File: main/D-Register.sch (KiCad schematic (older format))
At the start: 19 parts, among them U77 74LS245, U78 74LS173, U79 74LS173

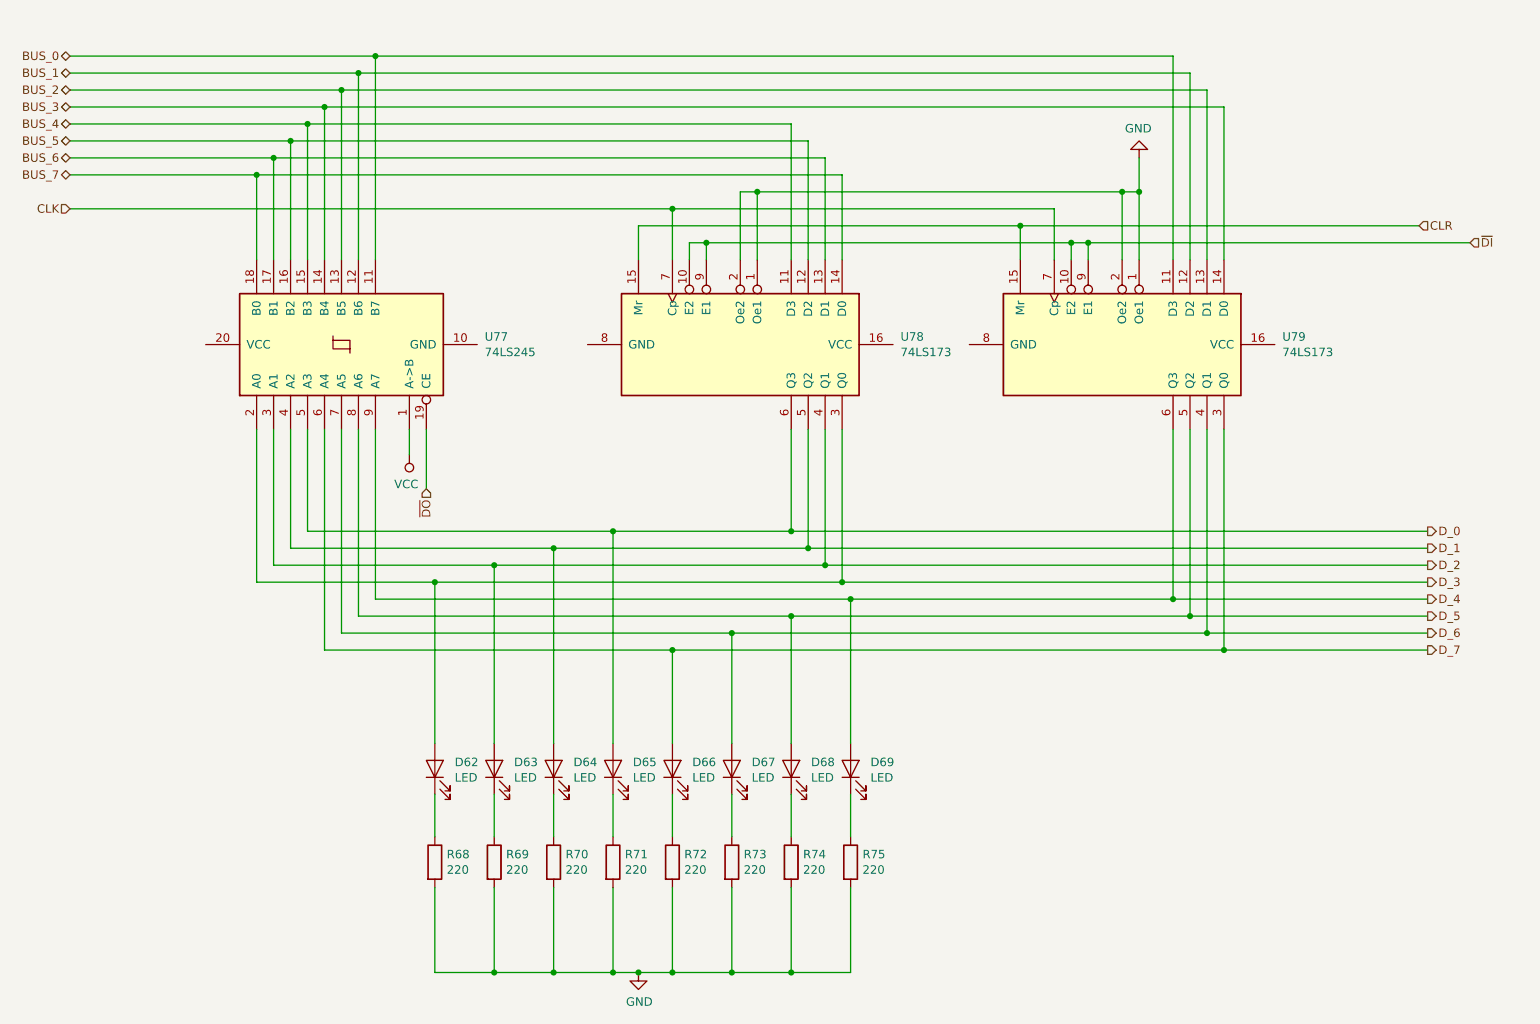
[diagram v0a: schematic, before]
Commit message: Replot main with symbols
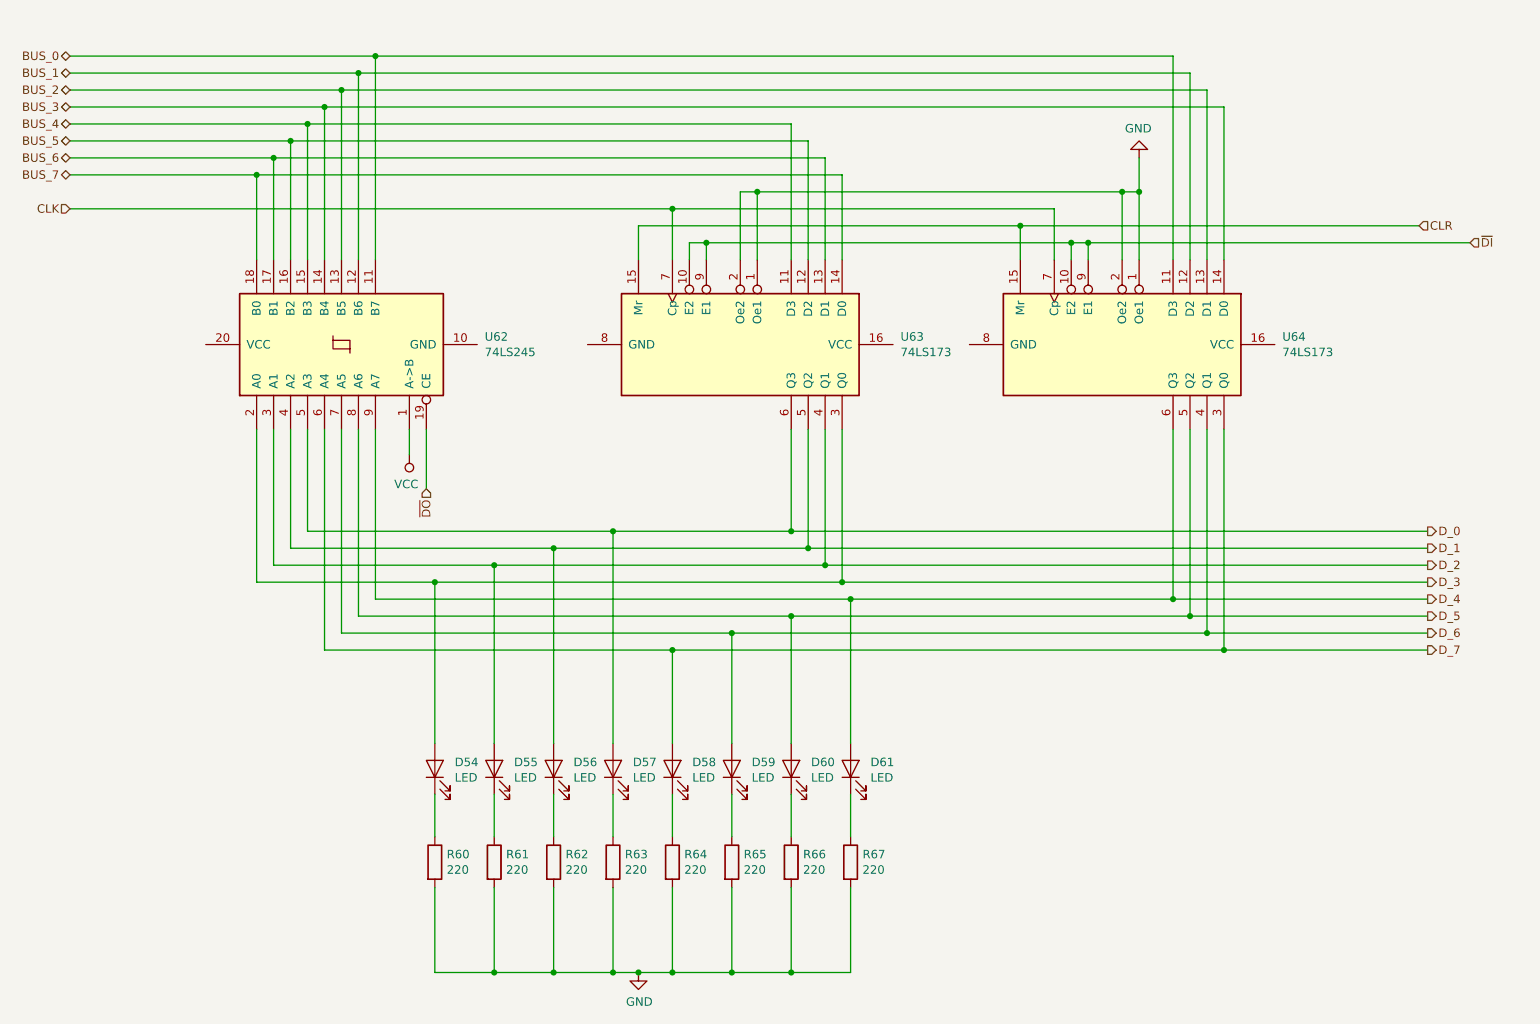
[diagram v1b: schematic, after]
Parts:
- renumbered D62 to D54, D63 to D55, D64 to D56, D65 to D57, D66 to D58, D67 to D59, D68 to D60, D69 to D61, R68 to R60, R69 to R61, R70 to R62, R71 to R63, R72 to R64, R73 to R65, R74 to R66, R75 to R67, U77 to U62, U78 to U63, U79 to U64
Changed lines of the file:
@@
 Sheet 17 26
 Title "D Register"
-Date "2019-11-13"
+Date "2019-11-17"
 Rev "v1.0"
 Comp "Christopher Milan"
@@
 AR Path="/5D9C73BD/5DA1765F" Ref="U?"  Part="1"
 AR Path="/5D9E82CE/5DA1765F" Ref="U?"  Part="1"
-AR Path="/5DA98D6D/5DA9A587/5DA1765F" Ref="U78"  Part="1"
-F 0 "U78" V 5204 4044 50  0000 L CNN
+AR Path="/5DA98D6D/5DA9A587/5DA1765F" Ref="U63"  Part="1"
+F 0 "U63" V 5204 4044 50  0000 L CNN
 F 1 "74LS173" V 5295 4044 50  0000 L CNN
 F 2 "" H 5250 3100 50  0001 C CNN
@@
 AR Path="/5D9C73BD/5DA1760E" Ref="R?"  Part="1"
 AR Path="/5D9E82CE/5DA1760E" Ref="R?"  Part="1"
-AR Path="/5DA98D6D/5DA9A587/5DA1760E" Ref="R75"  Part="1"
-F 0 "R75" H 5970 6196 50  0000 L CNN
+AR Path="/5DA98D6D/5DA9A587/5DA1760E" Ref="R67"  Part="1"
+F 0 "R67" H 5970 6196 50  0000 L CNN
 F 1 "220" H 5970 6105 50  0000 L CNN
 F 2 "" V 5830 6150 50  0001 C CNN
@@
 AR Path="/5D9C73BD/5DA17608" Ref="R?"  Part="1"
 AR Path="/5D9E82CE/5DA17608" Ref="R?"  Part="1"
-AR Path="/5DA98D6D/5DA9A587/5DA17608" Ref="R74"  Part="1"
-F 0 "R74" H 5620 6196 50  0000 L CNN
+AR Path="/5DA98D6D/5DA9A587/5DA17608" Ref="R66"  Part="1"
+F 0 "R66" H 5620 6196 50  0000 L CNN
 F 1 "220" H 5620 6105 50  0000 L CNN
 F 2 "" V 5480 6150 50  0001 C CNN
@@
 AR Path="/5D9C73BD/5DA17602" Ref="R?"  Part="1"
 AR Path="/5D9E82CE/5DA17602" Ref="R?"  Part="1"
-AR Path="/5DA98D6D/5DA9A587/5DA17602" Ref="R73"  Part="1"
-F 0 "R73" H 5270 6196 50  0000 L CNN
+AR Path="/5DA98D6D/5DA9A587/5DA17602" Ref="R65"  Part="1"
+F 0 "R65" H 5270 6196 50  0000 L CNN
 F 1 "220" H 5270 6105 50  0000 L CNN
 F 2 "" V 5130 6150 50  0001 C CNN
@@
 AR Path="/5D9C73BD/5DA175FC" Ref="R?"  Part="1"
 AR Path="/5D9E82CE/5DA175FC" Ref="R?"  Part="1"
-AR Path="/5DA98D6D/5DA9A587/5DA175FC" Ref="R72"  Part="1"
-F 0 "R72" H 4920 6196 50  0000 L CNN
+AR Path="/5DA98D6D/5DA9A587/5DA175FC" Ref="R64"  Part="1"
+F 0 "R64" H 4920 6196 50  0000 L CNN
 F 1 "220" H 4920 6105 50  0000 L CNN
 F 2 "" V 4780 6150 50  0001 C CNN
@@
 AR Path="/5D9C73BD/5DA175F6" Ref="R?"  Part="1"
 AR Path="/5D9E82CE/5DA175F6" Ref="R?"  Part="1"
-AR Path="/5DA98D6D/5DA9A587/5DA175F6" Ref="R71"  Part="1"
-F 0 "R71" H 4570 6196 50  0000 L CNN
+AR Path="/5DA98D6D/5DA9A587/5DA175F6" Ref="R63"  Part="1"
+F 0 "R63" H 4570 6196 50  0000 L CNN
 F 1 "220" H 4570 6105 50  0000 L CNN
 F 2 "" V 4430 6150 50  0001 C CNN
@@
 AR Path="/5D9C73BD/5DA175F0" Ref="R?"  Part="1"
 AR Path="/5D9E82CE/5DA175F0" Ref="R?"  Part="1"
-AR Path="/5DA98D6D/5DA9A587/5DA175F0" Ref="R70"  Part="1"
-F 0 "R70" H 4220 6196 50  0000 L CNN
+AR Path="/5DA98D6D/5DA9A587/5DA175F0" Ref="R62"  Part="1"
+F 0 "R62" H 4220 6196 50  0000 L CNN
 F 1 "220" H 4220 6105 50  0000 L CNN
 F 2 "" V 4080 6150 50  0001 C CNN
@@
 AR Path="/5D9C73BD/5DA175EA" Ref="R?"  Part="1"
 AR Path="/5D9E82CE/5DA175EA" Ref="R?"  Part="1"
-AR Path="/5DA98D6D/5DA9A587/5DA175EA" Ref="R69"  Part="1"
-F 0 "R69" H 3870 6196 50  0000 L CNN
+AR Path="/5DA98D6D/5DA9A587/5DA175EA" Ref="R61"  Part="1"
+F 0 "R61" H 3870 6196 50  0000 L CNN
 F 1 "220" H 3870 6105 50  0000 L CNN
 F 2 "" V 3730 6150 50  0001 C CNN
@@
 AR Path="/5D9C73BD/5DA175E4" Ref="R?"  Part="1"
 AR Path="/5D9E82CE/5DA175E4" Ref="R?"  Part="1"
-AR Path="/5DA98D6D/5DA9A587/5DA175E4" Ref="R68"  Part="1"
-F 0 "R68" H 3520 6196 50  0000 L CNN
+AR Path="/5DA98D6D/5DA9A587/5DA175E4" Ref="R60"  Part="1"
+F 0 "R60" H 3520 6196 50  0000 L CNN
 F 1 "220" H 3520 6105 50  0000 L CNN
 F 2 "" V 3380 6150 50  0001 C CNN
@@
 AR Path="/5D9C73BD/5DA175C8" Ref="D?"  Part="1"
 AR Path="/5D9E82CE/5DA175C8" Ref="D?"  Part="1"
-AR Path="/5DA98D6D/5DA9A587/5DA175C8" Ref="D69"  Part="1"
-F 0 "D69" V 5939 5483 50  0000 R CNN
+AR Path="/5DA98D6D/5DA9A587/5DA175C8" Ref="D61"  Part="1"
+F 0 "D61" V 5939 5483 50  0000 R CNN
 F 1 "LED" V 5848 5483 50  0000 R CNN
 F 2 "" H 5900 5600 50  0001 C CNN
@@
 AR Path="/5D9C73BD/5DA175C2" Ref="D?"  Part="1"
 AR Path="/5D9E82CE/5DA175C2" Ref="D?"  Part="1"
-AR Path="/5DA98D6D/5DA9A587/5DA175C2" Ref="D68"  Part="1"
-F 0 "D68" V 5589 5483 50  0000 R CNN
+AR Path="/5DA98D6D/5DA9A587/5DA175C2" Ref="D60"  Part="1"
+F 0 "D60" V 5589 5483 50  0000 R CNN
 F 1 "LED" V 5498 5483 50  0000 R CNN
 F 2 "" H 5550 5600 50  0001 C CNN
@@
 AR Path="/5D9C73BD/5DA175BC" Ref="D?"  Part="1"
 AR Path="/5D9E82CE/5DA175BC" Ref="D?"  Part="1"
-AR Path="/5DA98D6D/5DA9A587/5DA175BC" Ref="D67"  Part="1"
-F 0 "D67" V 5239 5483 50  0000 R CNN
+AR Path="/5DA98D6D/5DA9A587/5DA175BC" Ref="D59"  Part="1"
+F 0 "D59" V 5239 5483 50  0000 R CNN
 F 1 "LED" V 5148 5483 50  0000 R CNN
 F 2 "" H 5200 5600 50  0001 C CNN
@@
 AR Path="/5D9C73BD/5DA175B6" Ref="D?"  Part="1"
 AR Path="/5D9E82CE/5DA175B6" Ref="D?"  Part="1"
-AR Path="/5DA98D6D/5DA9A587/5DA175B6" Ref="D66"  Part="1"
-F 0 "D66" V 4889 5483 50  0000 R CNN
+AR Path="/5DA98D6D/5DA9A587/5DA175B6" Ref="D58"  Part="1"
+F 0 "D58" V 4889 5483 50  0000 R CNN
 F 1 "LED" V 4798 5483 50  0000 R CNN
 F 2 "" H 4850 5600 50  0001 C CNN
@@
 AR Path="/5D9C73BD/5DA175B0" Ref="D?"  Part="1"
 AR Path="/5D9E82CE/5DA175B0" Ref="D?"  Part="1"
-AR Path="/5DA98D6D/5DA9A587/5DA175B0" Ref="D65"  Part="1"
-F 0 "D65" V 4539 5483 50  0000 R CNN
+AR Path="/5DA98D6D/5DA9A587/5DA175B0" Ref="D57"  Part="1"
+F 0 "D57" V 4539 5483 50  0000 R CNN
 F 1 "LED" V 4448 5483 50  0000 R CNN
 F 2 "" H 4500 5600 50  0001 C CNN
@@
 AR Path="/5D9C73BD/5DA175AA" Ref="D?"  Part="1"
 AR Path="/5D9E82CE/5DA175AA" Ref="D?"  Part="1"
-AR Path="/5DA98D6D/5DA9A587/5DA175AA" Ref="D64"  Part="1"
-F 0 "D64" V 4189 5483 50  0000 R CNN
+AR Path="/5DA98D6D/5DA9A587/5DA175AA" Ref="D56"  Part="1"
+F 0 "D56" V 4189 5483 50  0000 R CNN
 F 1 "LED" V 4098 5483 50  0000 R CNN
 F 2 "" H 4150 5600 50  0001 C CNN
@@
 AR Path="/5D9C73BD/5DA175A4" Ref="D?"  Part="1"
 AR Path="/5D9E82CE/5DA175A4" Ref="D?"  Part="1"
-AR Path="/5DA98D6D/5DA9A587/5DA175A4" Ref="D63"  Part="1"
-F 0 "D63" V 3839 5483 50  0000 R CNN
+AR Path="/5DA98D6D/5DA9A587/5DA175A4" Ref="D55"  Part="1"
+F 0 "D55" V 3839 5483 50  0000 R CNN
 F 1 "LED" V 3748 5483 50  0000 R CNN
 F 2 "" H 3800 5600 50  0001 C CNN
@@
 AR Path="/5D9C73BD/5DA1759E" Ref="D?"  Part="1"
 AR Path="/5D9E82CE/5DA1759E" Ref="D?"  Part="1"
-AR Path="/5DA98D6D/5DA9A587/5DA1759E" Ref="D62"  Part="1"
-F 0 "D62" V 3489 5483 50  0000 R CNN
+AR Path="/5DA98D6D/5DA9A587/5DA1759E" Ref="D54"  Part="1"
+F 0 "D54" V 3489 5483 50  0000 R CNN
 F 1 "LED" V 3398 5483 50  0000 R CNN
 F 2 "" H 3450 5600 50  0001 C CNN
@@
 AR Path="/5D9C73BD/5DA17574" Ref="U?"  Part="1"
 AR Path="/5D9E82CE/5DA17574" Ref="U?"  Part="1"
-AR Path="/5DA98D6D/5DA9A587/5DA17574" Ref="U79"  Part="1"
-F 0 "U79" V 7454 4044 50  0000 L CNN
+AR Path="/5DA98D6D/5DA9A587/5DA17574" Ref="U64"  Part="1"
+F 0 "U64" V 7454 4044 50  0000 L CNN
 F 1 "74LS173" V 7545 4044 50  0000 L CNN
 F 2 "" H 7500 3100 50  0001 C CNN
@@
 AR Path="/5D9C73BD/5DA17547" Ref="U?"  Part="1"
 AR Path="/5D9E82CE/5DA17547" Ref="U?"  Part="1"
-AR Path="/5DA98D6D/5DA9A587/5DA17547" Ref="U77"  Part="1"
-F 0 "U77" V 2946 2256 50  0000 R CNN
+AR Path="/5DA98D6D/5DA9A587/5DA17547" Ref="U62"  Part="1"
+F 0 "U62" V 2946 2256 50  0000 R CNN
 F 1 "74LS245" V 2855 2256 50  0000 R CNN
 F 2 "" H 2900 3100 50  0001 C CNN

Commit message: Switch to using 74LS377 in place of two 74LS173
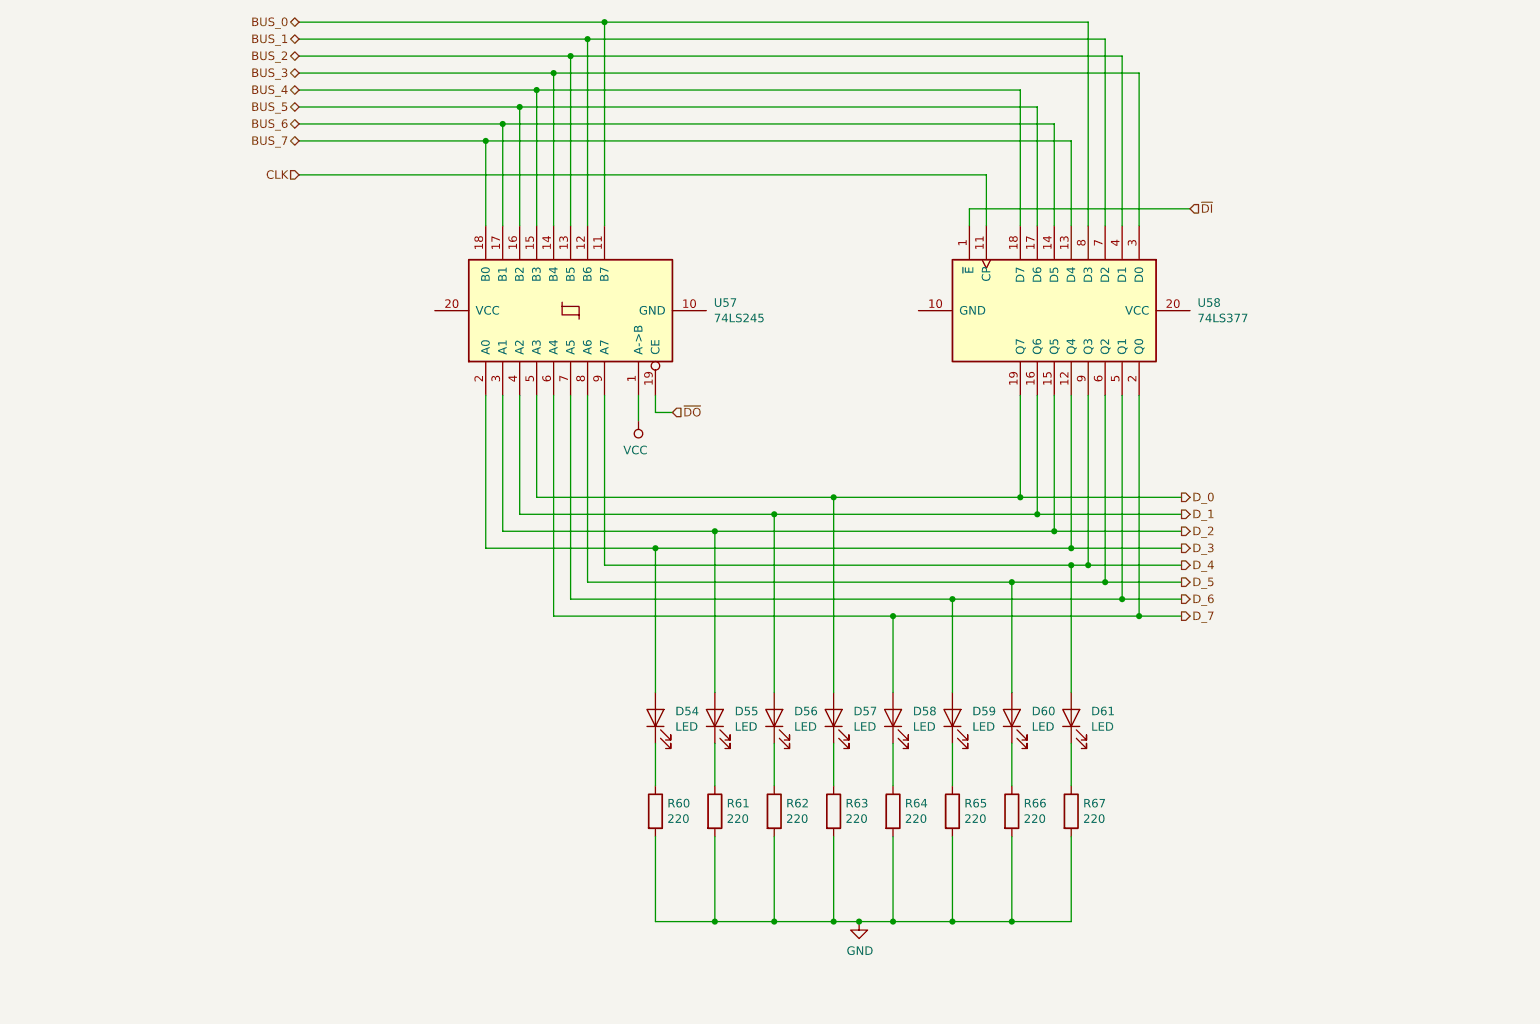
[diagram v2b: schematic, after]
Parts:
- removed U62: 74LS245, symbol 74xx:74LS245
- removed U63, U64: 74LS173, symbol 74xx:74LS173
- added U57: 74LS245, symbol 74xx:74LS245
- added U58: 74LS377, symbol 74xx:74LS377
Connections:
- net BUS_0: now also U57.11 (B7), U58.8 (D3)
- net BUS_1: now also U57.12 (B6), U58.7 (D2)
- net BUS_2: now also U57.13 (B5), U58.4 (D1)
- net BUS_3: now also U57.14 (B4), U58.3 (D0)
- net BUS_4: now also U57.15 (B3), U58.18 (D7)
- net BUS_5: now also U57.16 (B2), U58.17 (D6)
- net BUS_6: now also U57.17 (B1), U58.14 (D5)
- net BUS_7: now also U57.18 (B0), U58.13 (D4)
- net CLK: now also U58.11 (CP)
- net D_0: now also U57.5 (A3), U58.19 (Q7)
- net D_1: now also U57.4 (A2), U58.16 (Q6)
- net D_2: now also U57.3 (A1), U58.15 (Q5)
- net D_3: now also U57.2 (A0), U58.12 (Q4)
- net D_4: now also U57.9 (A7), U58.9 (Q3)
- net D_5: now also U57.8 (A6), U58.6 (Q2)
- net D_6: now also U57.7 (A5), U58.5 (Q1)
- net D_7: now also U57.6 (A4), U58.2 (Q0)
- net VCC: now also U57.1 (A->B)
- net ~DI~: now also U58.1 (~E)
- net ~DO~: now also U57.19 (CE)
